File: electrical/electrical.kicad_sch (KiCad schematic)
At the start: 0 parts

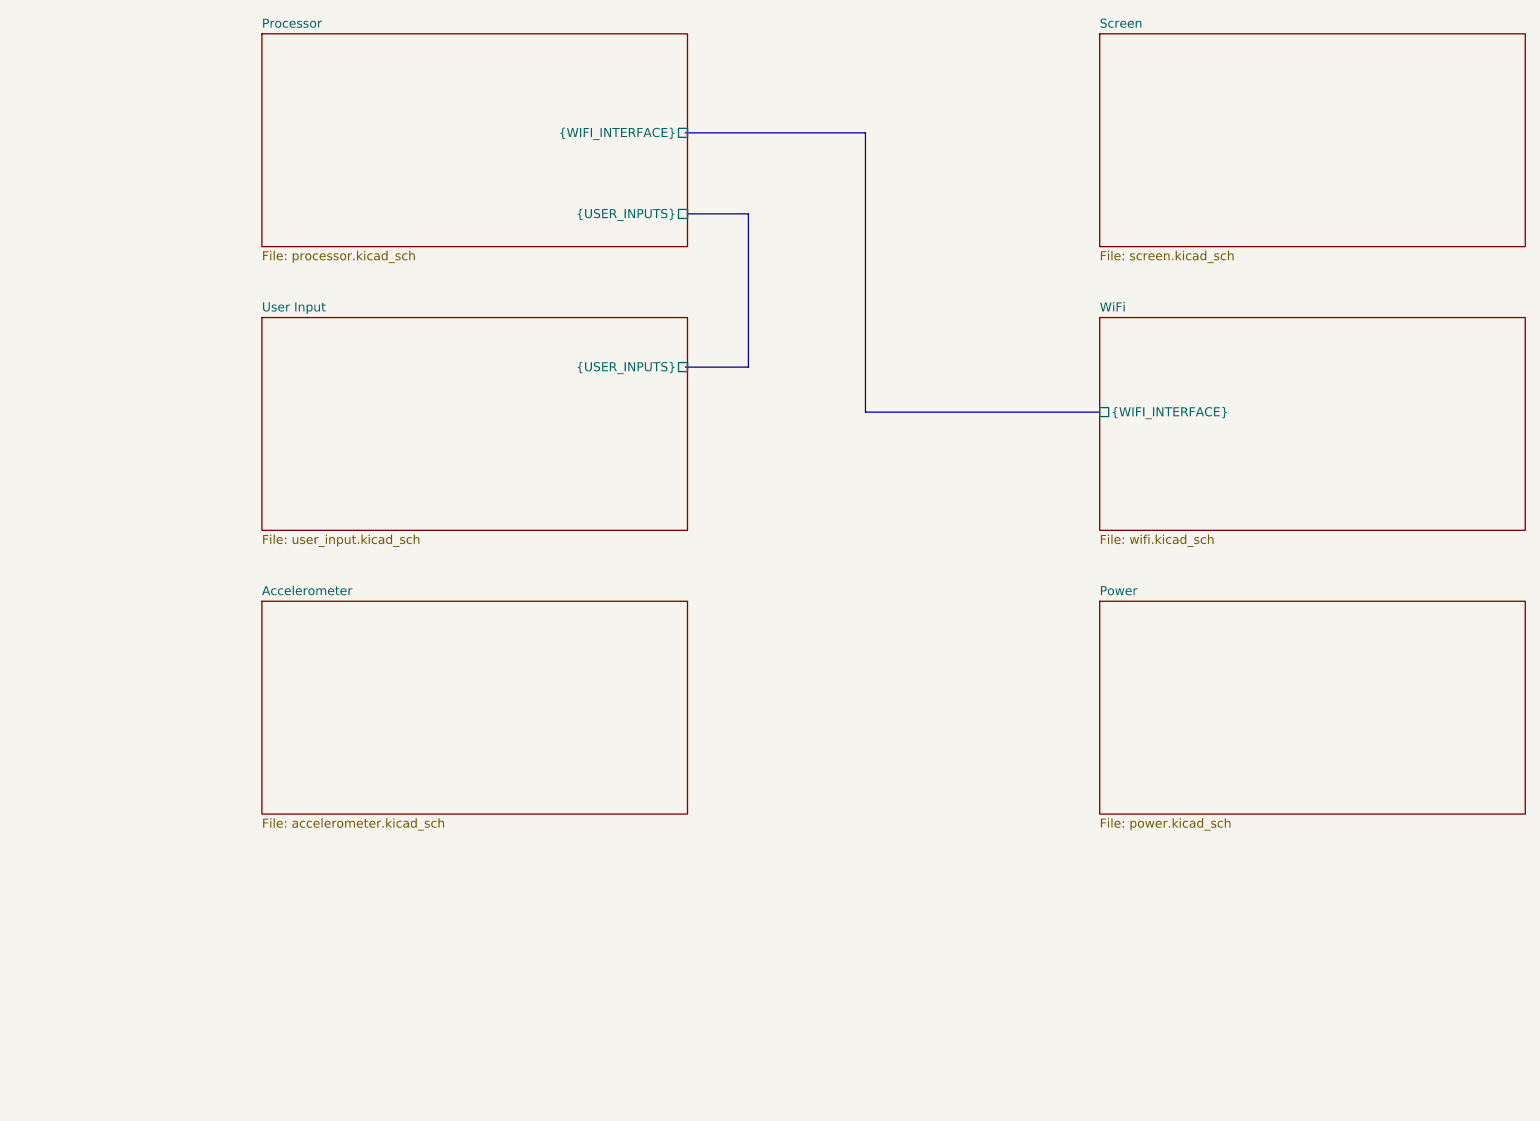
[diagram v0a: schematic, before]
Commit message: Completing schematic.
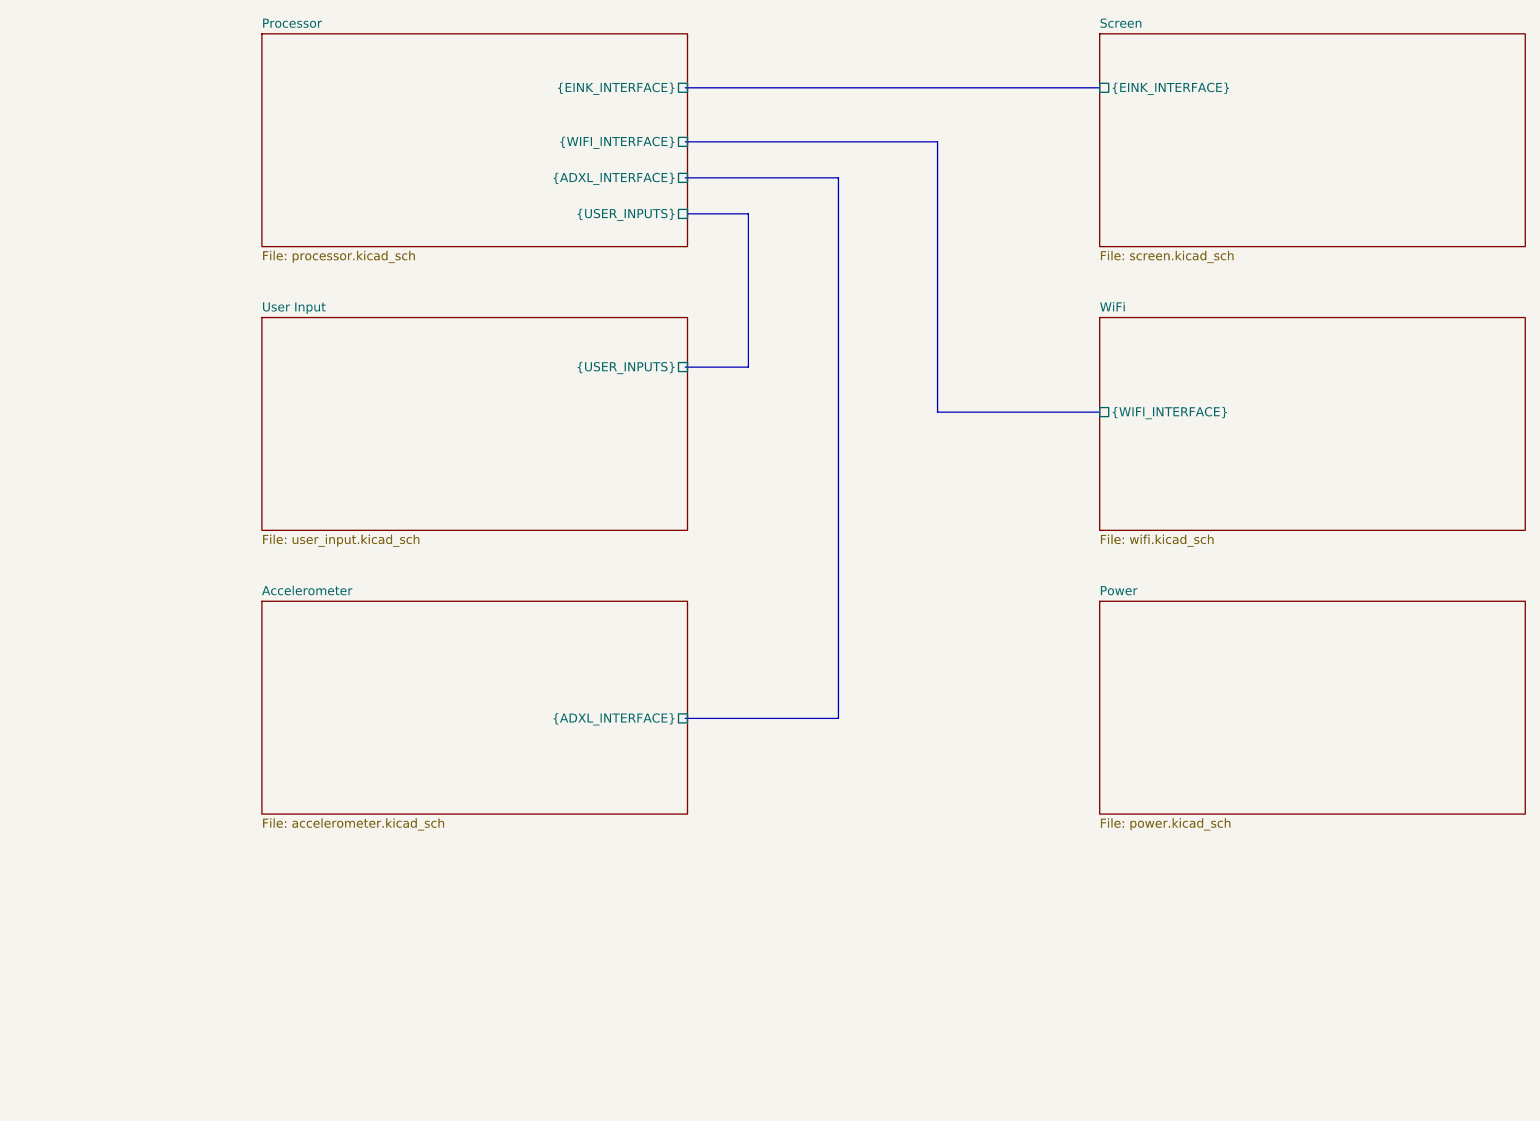
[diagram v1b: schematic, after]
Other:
- sheet Accelerometer ports: added {ADXL_INTERFACE}; removed none
- sheet Processor ports: added {ADXL_INTERFACE}, {EINK_INTERFACE}; removed none
- sheet Screen ports: added {EINK_INTERFACE}; removed none
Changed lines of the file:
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@@
 	(bus
 		(pts
-			(xy 142.24 53.34) (xy 142.24 92.71)
-		)
-		(stroke
-			(width 0)
-			(type default)
-		)
-	)
-	(bus
-		(pts
-			(xy 116.84 53.34) (xy 142.24 53.34)
-		)
-		(stroke
-			(width 0)
-			(type default)
-		)
-	)
-	(bus
-		(pts
-			(xy 142.24 92.71) (xy 175.26 92.71)
+			(xy 152.4 54.61) (xy 152.4 92.71)
+		)
+		(stroke
+			(width 0)
+			(type default)
+		)
+	)
+	(bus
+		(pts
+			(xy 116.84 54.61) (xy 152.4 54.61)
+		)
+		(stroke
+			(width 0)
+			(type default)
+		)
+	)
+	(bus
+		(pts
+			(xy 152.4 92.71) (xy 175.26 92.71)
+		)
+		(stroke
+			(width 0)
+			(type default)
+		)
+	)
+	(bus
+		(pts
+			(xy 116.84 59.69) (xy 138.43 59.69)
+		)
+		(stroke
+			(width 0)
+			(type default)
+		)
+	)
+	(bus
+		(pts
+			(xy 116.84 135.89) (xy 138.43 135.89)
+		)
+		(stroke
+			(width 0)
+			(type default)
+		)
+	)
+	(bus
+		(pts
+			(xy 116.84 46.99) (xy 175.26 46.99)
+		)
+		(stroke
+			(width 0)
+			(type default)
+		)
+	)
+	(bus
+		(pts
+			(xy 138.43 135.89) (xy 138.43 59.69)
 		)
 		(stroke
@@
 			)
 		)
+		(pin "{ADXL_INTERFACE}" passive
+			(at 117.15 135.89 0)
+			(effects
+				(font
+					(size 1.27 1.27)
+				)
+				(justify right)
+			)
+		)
 		(instances
 			(project "electrical"
@@
 		)
 		(pin "{WIFI_INTERFACE}" passive
-			(at 117.15 53.34 0)
+			(at 117.15 54.61 0)
 			(effects
 				(font
@@
 		(pin "{USER_INPUTS}" passive
 			(at 117.15 64.77 0)
+			(effects
+				(font
+					(size 1.27 1.27)
+				)
+				(justify right)
+			)
+		)
+		(pin "{ADXL_INTERFACE}" passive
+			(at 117.15 59.69 0)
+			(effects
+				(font
+					(size 1.27 1.27)
+				)
+				(justify right)
+			)
+		)
+		(pin "{EINK_INTERFACE}" passive
+			(at 117.15 46.99 0)
 			(effects
 				(font
@@
 			)
 		)
+		(pin "{EINK_INTERFACE}" passive
+			(at 175.26 46.99 180)
+			(effects
+				(font
+					(size 1.27 1.27)
+				)
+				(justify left)
+			)
+		)

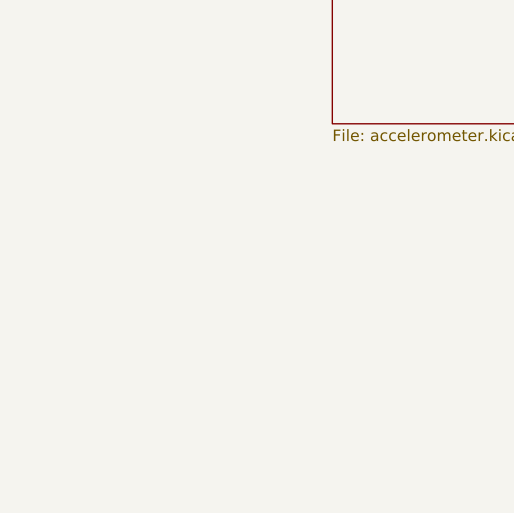
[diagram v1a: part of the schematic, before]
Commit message: Adding decoupling capacitors for STM.
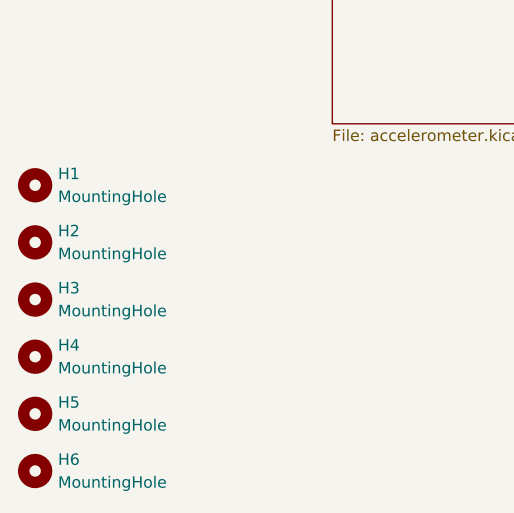
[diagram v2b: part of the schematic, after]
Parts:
- added H1, H2, H3, H4, H5, H6: MountingHole, MountingHole:MountingHole_2.2mm_M2, symbol Mechanical:MountingHole

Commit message: Completing PCB layout.
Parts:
- removed H5, H6: MountingHole, MountingHole:MountingHole_2.2mm_M2, symbol Mechanical:MountingHole
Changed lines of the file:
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@@
-	(symbol
-		(lib_id "Mechanical:MountingHole")
-		(at 24.13 181.61 0)
-		(unit 1)
-		(exclude_from_sim no)
-		(in_bom no)
-		(on_board yes)
-		(dnp no)
-		(fields_autoplaced yes)
-		(property "Reference" "H5"
-			(at 26.67 180.3399 0)
-			(effects
-				(font
-					(size 1.27 1.27)
-				)
-				(justify left)
-			)
-		)
-		(property "Value" "MountingHole"
-			(at 26.67 182.8799 0)
-			(effects
-				(font
-					(size 1.27 1.27)
-				)
-				(justify left)
-			)
-		)
-		(property "Footprint" "MountingHole:MountingHole_2.2mm_M2"
-			(at 24.13 181.61 0)
-			(effects
-				(font
-					(size 1.27 1.27)
-				)
-				(hide yes)
-			)
-		)
-		(property "Datasheet" "~"
-			(at 24.13 181.61 0)
-			(effects
-				(font
-					(size 1.27 1.27)
-				)
-				(hide yes)
-			)
-		)
-		(property "Description" "Mounting Hole without connection"
-			(at 24.13 181.61 0)
-			(effects
-				(font
-					(size 1.27 1.27)
-				)
-				(hide yes)
-			)
-		)
-		(instances
-			(project "electrical"
-				(path "/677117a5-2713-4117-9fd9-f2791321eb47"
-					(reference "H5")
-					(unit 1)
-				)
-			)
-		)
-	)
 	(symbol
 		(lib_id "Mechanical:MountingHole")
@@
 					(unit 1)
 				)
-			)
-		)
-	)
-	(symbol
-		(lib_id "Mechanical:MountingHole")
-		(at 24.13 187.96 0)
-		(unit 1)
-		(exclude_from_sim no)
-		(in_bom no)
-		(on_board yes)
-		(dnp no)
-		(fields_autoplaced yes)
-		(property "Reference" "H6"
-			(at 26.67 186.6899 0)
-			(effects
-				(font
-					(size 1.27 1.27)
-				)
-				(justify left)
-			)
-		)
-		(property "Value" "MountingHole"
-			(at 26.67 189.2299 0)
-			(effects
-				(font
-					(size 1.27 1.27)
-				)
-				(justify left)
-			)
-		)
-		(property "Footprint" "MountingHole:MountingHole_2.2mm_M2"
-			(at 24.13 187.96 0)
-			(effects
-				(font
-					(size 1.27 1.27)
-				)
-				(hide yes)
-			)
-		)
-		(property "Datasheet" "~"
-			(at 24.13 187.96 0)
-			(effects
-				(font
-					(size 1.27 1.27)
-				)
-				(hide yes)
-			)
-		)
-		(property "Description" "Mounting Hole without connection"
-			(at 24.13 187.96 0)
-			(effects
-				(font
-					(size 1.27 1.27)
-				)
-				(hide yes)
-			)
-		)
-		(instances
-			(project "electrical"
-				(path "/677117a5-2713-4117-9fd9-f2791321eb47"
-					(reference "H6")
-					(unit 1)
-				)

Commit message: Updating schematic pages.
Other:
- company: (none) -> github.com/AdrianTheHacker
- title: (none) -> Etchasketch System Layout
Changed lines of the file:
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@@
 	(generator_version "9.0")
 	(paper "A4")
+	(title_block
+		(title "Etchasketch System Layout")
+		(date "2025-12-10")
+		(rev "2.0")
+		(company "github.com/AdrianTheHacker")
+	)
 	(bus
 		(pts
